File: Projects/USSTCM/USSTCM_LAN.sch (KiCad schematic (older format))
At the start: 54 parts, among them IC3 RASPI_LAN9514, IC5 FSUSB42MSOP10, Q3 DMG1012T

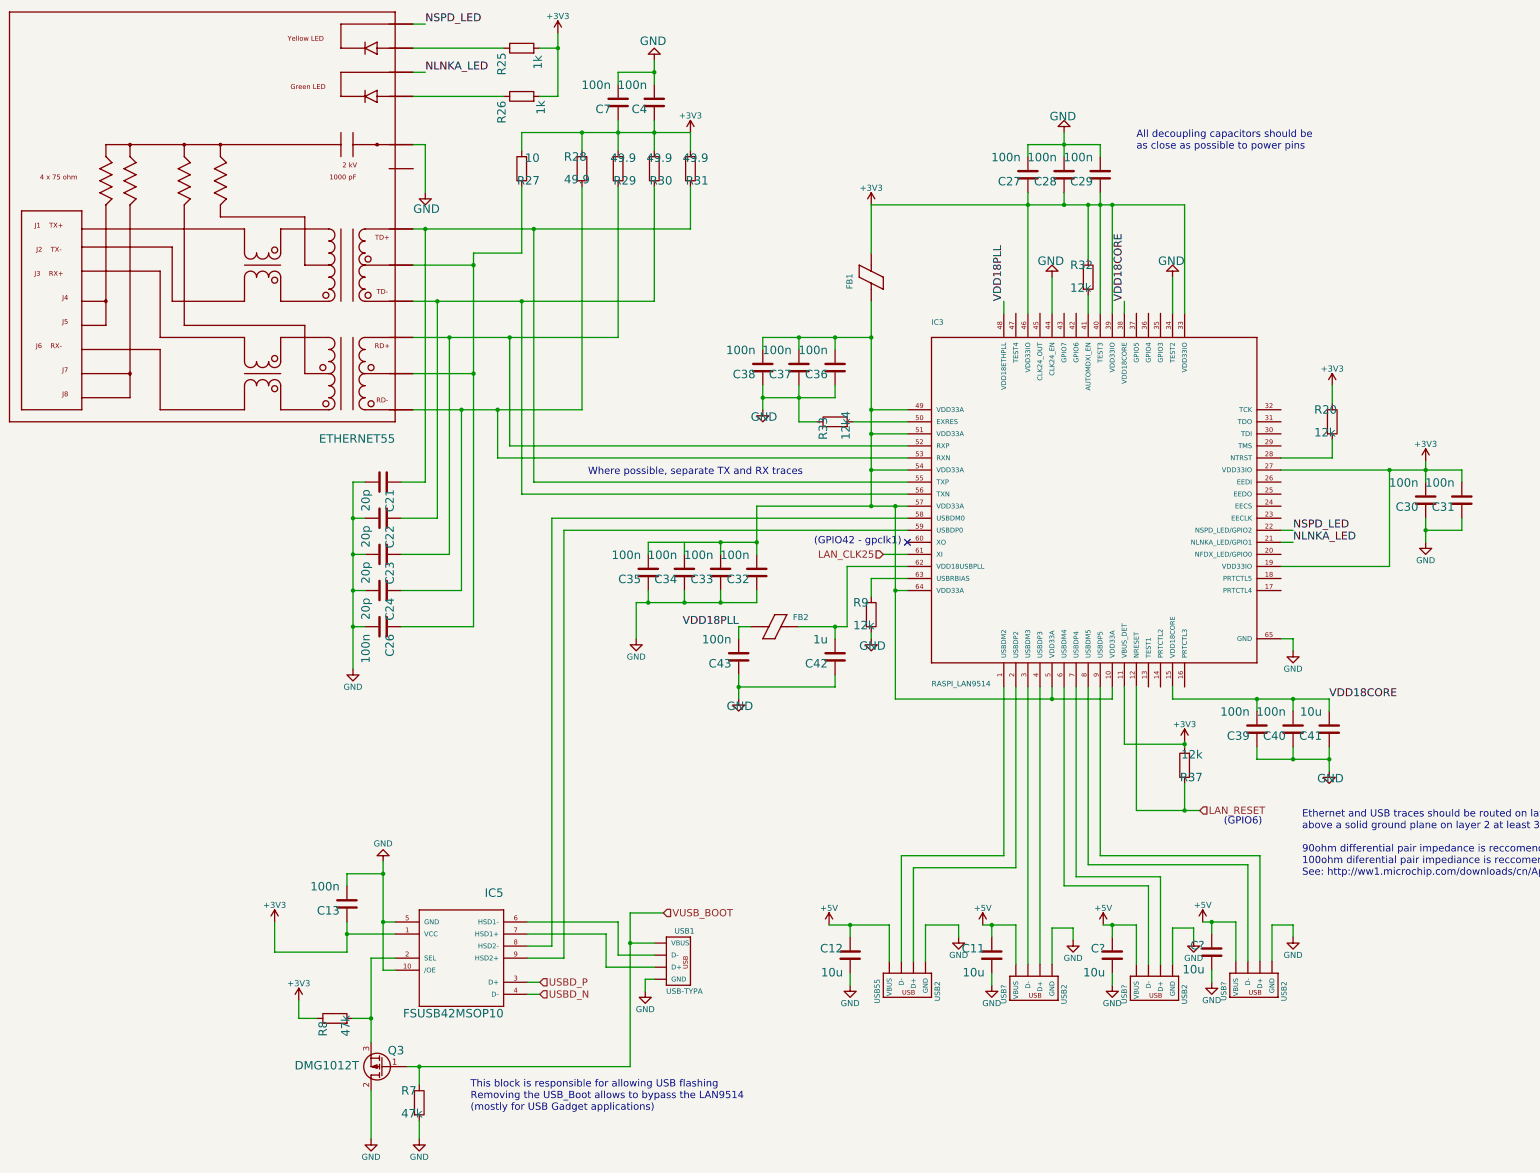
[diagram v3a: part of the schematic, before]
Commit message: added differential routes
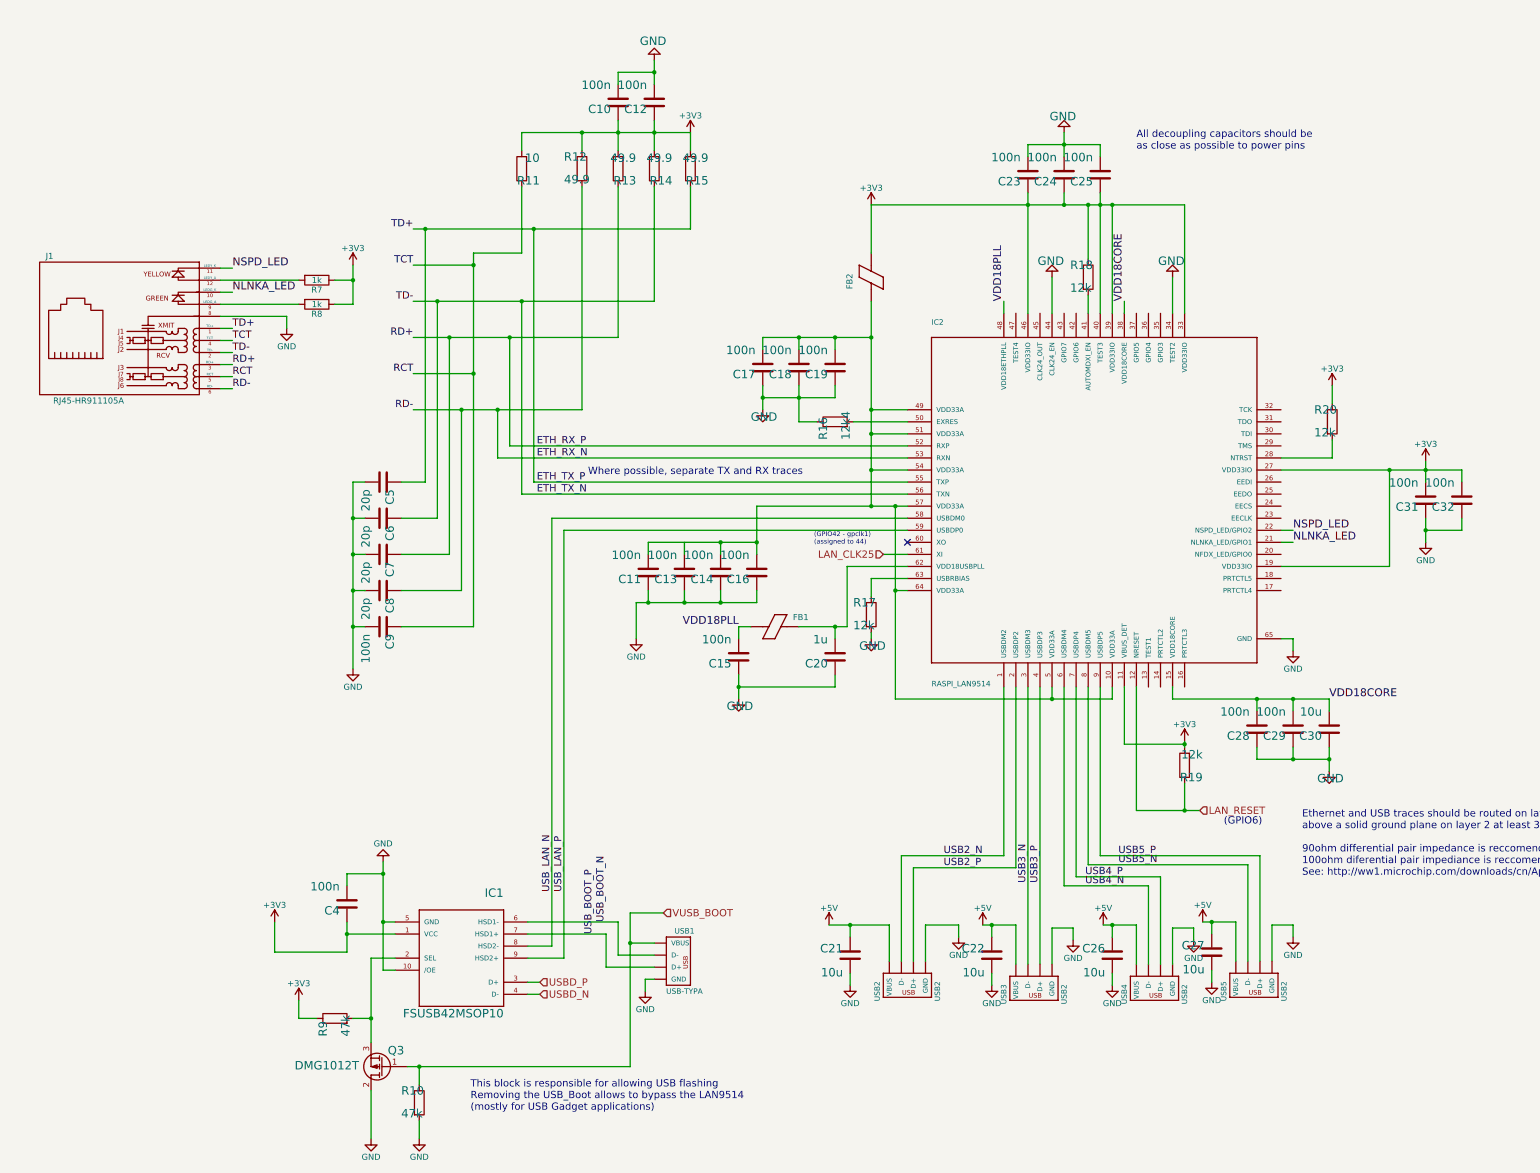
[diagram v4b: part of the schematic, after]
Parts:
- removed ETHERNET55: HR911105A, USSTCM:HANRUN_RJ45, symbol HANRUN-HR911105A
- added J1: RJ45-HR911105A, USSTCM:HANRUN_RJ45, symbol RJ45-HR911105A
- C10: renamed from C7; footprint USSTCM:RCL_C0603 -> Capacitors_SMD:C_0805
- C11: renamed from C35; footprint USSTCM:RCL_C0603 -> Capacitors_SMD:C_0805
- C12: renamed from C4; footprint USSTCM:RCL_C0603 -> Capacitors_SMD:C_0805
- C13: renamed from C34; footprint USSTCM:RCL_C0603 -> Capacitors_SMD:C_0805
- C14: renamed from C33; footprint USSTCM:RCL_C0603 -> Capacitors_SMD:C_0805
- C15: renamed from C43; footprint USSTCM:RCL_C0603 -> Capacitors_SMD:C_0805
- C16: renamed from C32; footprint USSTCM:RCL_C0603 -> Capacitors_SMD:C_0805
- C17: renamed from C38; footprint USSTCM:RCL_C0603 -> Capacitors_SMD:C_0805
- C18: renamed from C37; footprint USSTCM:RCL_C0603 -> Capacitors_SMD:C_0805
- C19: renamed from C36; footprint USSTCM:RCL_C0603 -> Capacitors_SMD:C_0805
- C20: renamed from C42; footprint USSTCM:RCL_C0805 -> Capacitors_SMD:C_0805
- C21: renamed from C12; footprint USSTCM:RCL_C0805 -> Capacitors_SMD:C_0805
- C22: renamed from C11; footprint USSTCM:RCL_C0805 -> Capacitors_SMD:C_0805
- C23: renamed from C27; footprint USSTCM:RCL_C0603 -> Capacitors_SMD:C_0805
- C24: renamed from C28; footprint USSTCM:RCL_C0603 -> Capacitors_SMD:C_0805
- C25: renamed from C29; footprint USSTCM:RCL_C0603 -> Capacitors_SMD:C_0805
- C26, C27: renamed from C?; footprint USSTCM:RCL_C0805 -> Capacitors_SMD:C_0805
- C28: renamed from C39; footprint USSTCM:RCL_C0603 -> Capacitors_SMD:C_0805
- C29: renamed from C40; footprint USSTCM:RCL_C0603 -> Capacitors_SMD:C_0805
- C30: renamed from C41; footprint USSTCM:RCL_C0805 -> Capacitors_SMD:C_0805
- C31: renamed from C30; footprint USSTCM:RCL_C0603 -> Capacitors_SMD:C_0805
- C32: renamed from C31; footprint USSTCM:RCL_C0603 -> Capacitors_SMD:C_0805
- C4: renamed from C13; footprint USSTCM:RCL_C0603 -> Capacitors_SMD:C_0805
- C5: renamed from C21; footprint USSTCM:RCL_C0603 -> Capacitors_SMD:C_0805
- C6: renamed from C22; footprint USSTCM:RCL_C0603 -> Capacitors_SMD:C_0805
- C7: renamed from C23; footprint USSTCM:RCL_C0603 -> Capacitors_SMD:C_0805
- C8: renamed from C24; footprint USSTCM:RCL_C0603 -> Capacitors_SMD:C_0805
- C9: renamed from C26; footprint USSTCM:RCL_C0603 -> Capacitors_SMD:C_0805
- FB1: renamed from FB2; footprint USSTCM:RASPI_C0805 -> Capacitors_SMD:C_0805
- FB2: renamed from FB1; footprint USSTCM:RASPI_C0805 -> Capacitors_SMD:C_0805
- IC1: renamed from IC5; footprint USSTCM:RASPI_MSOP10 -> Housings_SSOP:MSOP-10_3x3mm_Pitch0.5mm
- IC2: renamed from IC3; footprint USSTCM:RASPI_QFN64-9X9 -> Housings_DFN_QFN:QFN-64-1EP_9x9mm_Pitch0.5mm
- R10: renamed from R7; footprint USSTCM:RCL_R0603 -> Resistors_SMD:R_0805
- R11: renamed from R27; footprint USSTCM:RCL_R0603 -> Resistors_SMD:R_0805
- R12: renamed from R28; footprint USSTCM:RCL_R0603 -> Resistors_SMD:R_0805
- R13: renamed from R29; footprint USSTCM:RCL_R0603 -> Resistors_SMD:R_0805
- R14: renamed from R30; footprint USSTCM:RCL_R0603 -> Resistors_SMD:R_0805
- R15: renamed from R31; footprint USSTCM:RCL_R0603 -> Resistors_SMD:R_0805
- R16: renamed from R33; footprint USSTCM:RCL_R0603 -> Resistors_SMD:R_0805
- R17: renamed from R9; footprint USSTCM:RCL_R0603 -> Resistors_SMD:R_0805
- R18: renamed from R32; footprint USSTCM:RCL_R0603 -> Resistors_SMD:R_0805
- R19: renamed from R37; footprint USSTCM:RCL_R0603 -> Resistors_SMD:R_0805
- R20: footprint USSTCM:RCL_R0603 -> Resistors_SMD:R_0805
- R7: renamed from R25; footprint USSTCM:RCL_R0603 -> Resistors_SMD:R_0805
- R8: renamed from R26; footprint USSTCM:RCL_R0603 -> Resistors_SMD:R_0805
- R9: renamed from R8; footprint USSTCM:RCL_R0603 -> Resistors_SMD:R_0805
- USB1: footprint USB-A-F-PTH -> USST-footprints:MINI-B-USBR
- USB2: renamed from USB55; footprint USSTCM:RASPI_USB2 -> USST-footprints:USB-A-UPRIGHT
- USB3, USB4, USB5: renamed from USB?; footprint USSTCM:RASPI_USB2 -> USST-footprints:USB-A-UPRIGHT
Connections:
- net +3V3: now also R7.1, R8.1; no longer R7.2, R8.2
- net GND: now also J1.8
- net NLNKA_LED: now also J1.10 (LEDG_K)
- net NSPD_LED: now also J1.11 (LEDY_K)
- net ETH_TX_P: now reaches C5.1, IC2.55 (TXP), R15.1
- net ETH_TX_P: now also J1.1 (TD+)
- net ETH_TX_N: now reaches C6.1, IC2.56 (TXN), R14.1
- net ETH_TX_N: now also J1.2 (TD-)
- net ETH_RX_P: now reaches C7.1, IC2.52 (RXP), R13.1
- net ETH_RX_P: now also J1.3 (RD+)
- net ETH_RX_N: now reaches C8.1, IC2.53 (RXN), R12.2
- net ETH_RX_N: now also J1.6 (RD-)
- net RCT: now reaches C9.1, R11.1
- net RCT: now also J1.4 (TCT), J1.5 (RCT)
- net USB_BOOT_N: now reaches IC1.6 (HSD1-), USB1.D-
- net USB_BOOT_P: now reaches IC1.7 (HSD1+), USB1.D+
- net USB_LAN_N: now reaches IC1.8 (HSD2-), IC2.58 (USBDM0)
- net USB_LAN_P: now reaches IC1.9 (HSD2+), IC2.59 (USBDP0)
- net USB3_P: now reaches IC2.4 (USBDP3), USB3.D+
- net USB3_N: now reaches IC2.3 (USBDM3), USB3.D-
- net USB2_P: now reaches IC2.2 (USBDP2), USB2.D+
- net USB2_N: now reaches IC2.1 (USBDM2), USB2.D-
- net USB4_N: now reaches IC2.6 (USBDM4), USB4.D-
- net USB4_P: now reaches IC2.7 (USBDP4), USB4.D+
- net USB5_N: now reaches IC2.8 (USBDM5), USB5.D-
- net USB5_P: now reaches IC2.9 (USBDP5), USB5.D+
- new net: J1.12 (LEDY_A), R7.2
- new net: J1.9 (LEDG_A), R8.2
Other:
- note added: "(GPIO42 - gpclk1)\n(assigned to 44)"
- note removed: "(GPIO42 - gpclk1)"
- moved on the sheet: R7, R8
